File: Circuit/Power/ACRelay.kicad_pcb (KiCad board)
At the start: 2 copper layers, 25.4 x 20.3 mm, 13 parts, among them J1 Input, J2 Output, Q1 RFP30N06LE, Q2 RFP30N06LE, U2 PC817

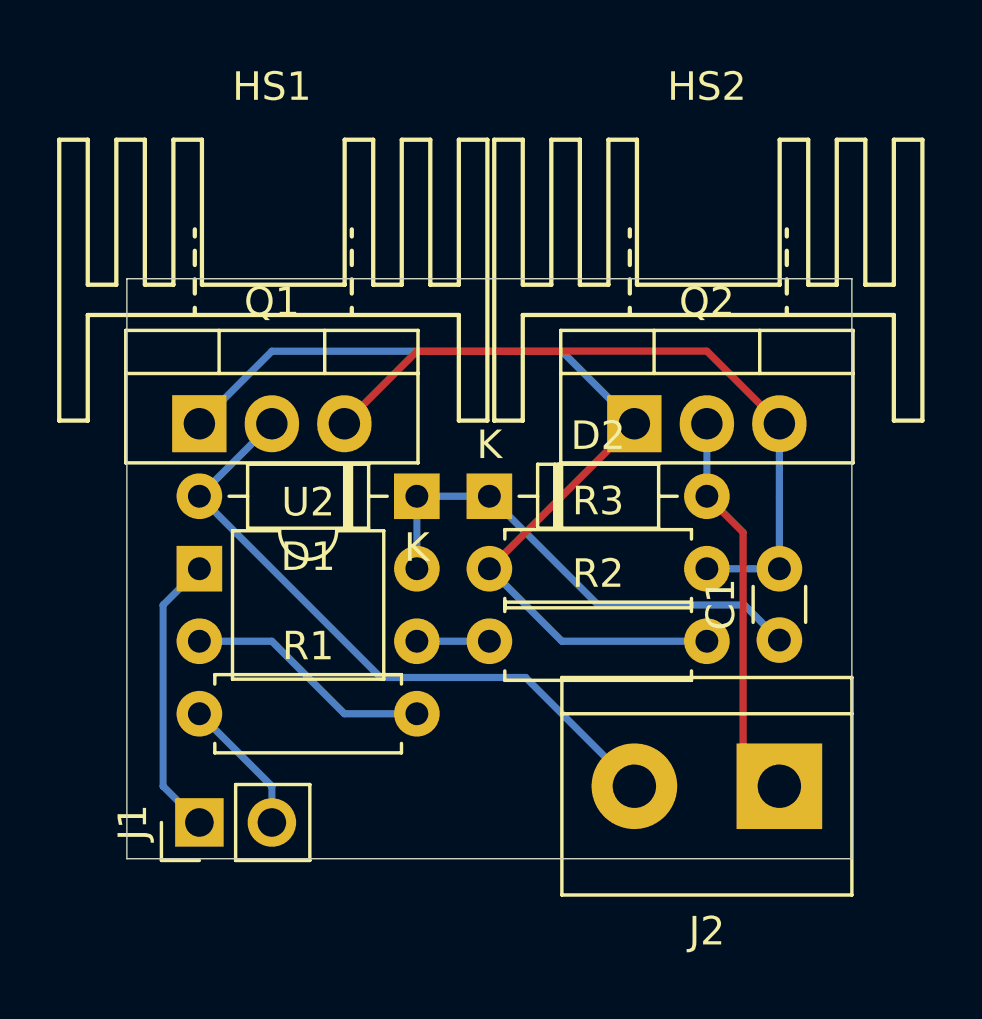
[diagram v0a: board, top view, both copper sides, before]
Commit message: [Circuit] Add DC relay design
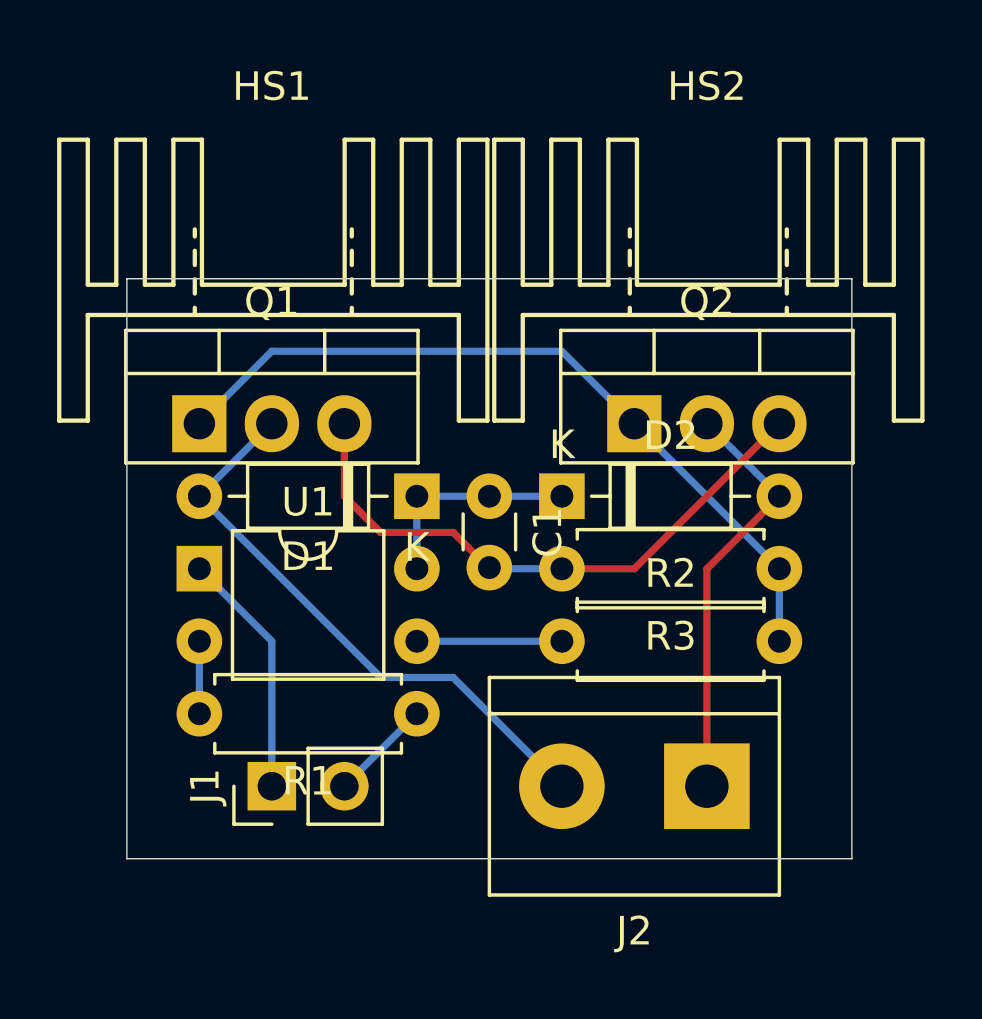
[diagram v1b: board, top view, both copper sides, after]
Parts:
- moved C1 11.3 mm to (73.7, 50.8), turned to 270 degrees
- moved R3 10.2 mm to (83.8, 53.3), turned to 180 degrees
- moved R1 7.62 mm to (71.1, 58.4), turned to 180 degrees
- moved J1 2.84 mm to (66.0, 61.0)
- moved D2 2.54 mm to (76.2, 50.8)
- moved R2 2.54 mm to (76.2, 55.9)
- moved J2 2.54 mm to (81.3, 61.0)
- renumbered U2 to U1
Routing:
- net Net-(C1-Pad1): track 17.4 -> 7.62 mm
- net Net-(R1-Pad2): track 8.67 -> 2.54 mm
- net Net-(Q1-Pad1): track 33.2 -> 27.1 mm
- net Net-(C1-Pad2): track 25.0 -> 21.0 mm
- net Net-(R2-Pad1): track 2.54 -> 5.08 mm
- net /Output1: track 23.0 -> 20.5 mm
- net /Input+: track 9.94 -> 8.67 mm
- net /Input-: track 4.86 -> 3.59 mm
- net /Output2: track 13.8 -> 14.8 mm

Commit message: [Circuit] Fine tune some pcb layouts
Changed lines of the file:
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@@
     (thickness 1.6)
     (drawings 4)
-    (tracks 31)
+    (tracks 27)
     (zones 0)
     (modules 13)
@@
   (segment (start 63.5 55.88) (end 63.5 58.42) (width 0.25) (layer B.Cu) (net 1) (status 30))
   (segment (start 71.12 53.34) (end 71.12 50.8) (width 0.25) (layer B.Cu) (net 3) (status 30))
-  (segment (start 73.62 53.34) (end 73.66 53.3) (width 0.25) (layer B.Cu) (net 2) (status 30))
-  (segment (start 73.66 53.3) (end 73.7 53.3) (width 0.25) (layer B.Cu) (net 2) (status 30))
-  (segment (start 73.7 53.34) (end 73.66 53.3) (width 0.25) (layer B.Cu) (net 2) (status 30))
   (segment (start 76.2 53.34) (end 73.7 53.34) (width 0.25) (layer B.Cu) (net 2) (status 30))
-  (segment (start 73.66 53.3) (end 73.62 53.3) (width 0.25) (layer F.Cu) (net 2) (status 30))
   (segment (start 73.62 53.3) (end 72.39 52.07) (width 0.25) (layer F.Cu) (net 2) (status 10))
   (segment (start 78.74 53.34) (end 83.82 48.26) (width 0.25) (layer F.Cu) (net 2) (status 20))
